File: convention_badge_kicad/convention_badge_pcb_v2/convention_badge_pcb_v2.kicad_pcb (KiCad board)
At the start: 2 copper layers, 5 parts, among them J2 ER-CON24HT-1, J3 3.7V Battery, SW4 SW_SPST, U1 ESP32-C3-WROOM-02

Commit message: schematic minus e paper integration complete
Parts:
- added C1: 1uf, PCM_JLCPCB:C_0603, F.Cu at (122.7, 65.8)
- added C2: 0.1uf, PCM_JLCPCB:C_0603, F.Cu at (122.7, 68.1)
- added C3: 10uf, PCM_JLCPCB:C_0603, F.Cu at (122.7, 70.3)
- added C4: 10uf, PCM_JLCPCB:C_0603, F.Cu at (122.7, 72.6)
- added C5: 0.1uF, PCM_JLCPCB:C_0603, F.Cu at (122.7, 74.8)
- added C6: 2.2uF, PCM_JLCPCB:C_0603, F.Cu at (122.7, 77.1)
- added C7: 100uF, PCM_JLCPCB:C_0603, F.Cu at (122.7, 79.3)
- added C8: 2.2uF, PCM_JLCPCB:C_0603, F.Cu at (122.7, 81.6)
- added C9: 0.1uF, PCM_JLCPCB:C_0603, F.Cu at (122.7, 83.8)
- added D2: LED, PCM_JLCPCB:D_0603, F.Cu at (179.4, 76.7)
- added D3: SS14, PCM_JLCPCB:D_DO-214AC(SMA), F.Cu at (100.0, 109.0)
- added DISP1: EPaper Breakout, 2_Displays:2.9_e_paper_ER-EPD029-2-5073, F.Cu at (83.6, 118.8)
- added J1: USBC, Connector_USB:USB_C_Receptacle_GCT_USB4105-xx-A_16P_TopMnt_Horizontal, F.Cu at (87.0, 101.0)
- added Q1: LP0404N3T5G, Package_TO_SOT_SMD:SOT-883, F.Cu at (178.0, 81.3)
- added R1: 5.1k, PCM_JLCPCB:R_0603, F.Cu at (131.6, 65.8)
- added R10: 100k, PCM_JLCPCB:R_0603, F.Cu at (135.2, 72.6)
- added R2: 5.1k, PCM_JLCPCB:R_0603, F.Cu at (131.6, 68.1)
- added R3: 10k, PCM_JLCPCB:R_0603, F.Cu at (131.6, 70.3)
- added R4: 10k, PCM_JLCPCB:R_0603, F.Cu at (131.6, 72.6)
- added R5: 1k, PCM_JLCPCB:R_0603, F.Cu at (131.6, 74.8)
- added R6: 1k, PCM_JLCPCB:R_0603, F.Cu at (131.6, 77.1)
- added R7: 10k, PCM_JLCPCB:R_0603, F.Cu at (135.2, 65.8)
- added R8: 100, PCM_JLCPCB:R_0603, F.Cu at (135.2, 68.1)
- added R9: 1k, PCM_JLCPCB:R_0603, F.Cu at (135.2, 70.3)
- added SW1: SW4X2, PCM_JLCPCB:SW-SMD_4P-L5.1-W5.1-P3.70-LS6.5-TL-2, F.Cu at (150.7, 97.2)
- added SW2: SW4X2, PCM_JLCPCB:SW-SMD_4P-L5.1-W5.1-P3.70-LS6.5-TL-2, F.Cu at (151.0, 104.0)
- added SW3: SW_Push, Button_Switch_THT:SW_PUSH_6mm, F.Cu at (176.5, 107.5)
- added SW5: SW_Push, Button_Switch_THT:SW_PUSH_6mm, F.Cu at (155.5, 148.5)
- added SW6: SW_SPST, Button_Switch_THT:SW_Slide-03_Wuerth-WS-SLTV_10x2.5x6.4_P2.54mm, F.Cu at (170.9, 82.1)
- added SW7: SW_Push, Button_Switch_THT:SW_PUSH_6mm, F.Cu at (124.5, 147.8)
- added SW8: SW_Push, Button_Switch_THT:SW_PUSH_6mm, F.Cu at (86.8, 146.8)
- added U2: FS8205A, Package_TO_SOT_SMD:SOT-23-6, F.Cu at (127.2, 67.1)
- added U3: TP4056, PCM_JLCPCB:ESOP-8_L4.9-W3.9-P1.27-LS6.0-BL-EP, F.Cu at (161.3, 68.7)
- added U4: DW01A, Package_TO_SOT_SMD:SOT-23-6, F.Cu at (127.2, 71.8)
- added U5: TLV75733PDBV, Package_TO_SOT_SMD:SOT-23-5, F.Cu at (127.2, 76.4)
- D1: value EPaper Display -> LED; footprint 2_Displays:2.9_e_paper_ER-EPD029-2-5073 -> PCM_JLCPCB:D_0603
- J2: value ER-CON24HT-1 -> EPaper; moved to B.Cu
- SW4: value SW_SPST -> SW_Push; footprint Button_Switch_THT:SW_Slide-03_Wuerth-WS-SLTV_10x2.5x6.4_P2.54mm -> Button_Switch_THT:SW_PUSH_6mm
- U1: moved to B.Cu
- moved D1 124.6 mm to (179.4, 74.1)
- moved SW4 85.7 mm to (175.5, 95.5)
- moved J2 82.4 mm to (168.6, 124.3), turned to 90 degrees
- moved J3 64.5 mm to (150.0, 114.5)
- moved U1 58.0 mm to (127.0, 100.6), turned to 180 degrees
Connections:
- D1 pad 1: +3.3V -> Net-(D1-K)
- D1 pad 2: GND -> /VUSB
- J3 pad 1: +3.7V -> Net-(J3-Pin_1)
- J3 pad 2: GND -> Net-(J3-Pin_2)
- SW4 pad 1: unconnected-(SW4-A-Pad1) -> /GPIO1
- SW4 pad 2: +3.7V -> GND
- U1 pad 11: unconnected-(U1-GPIO20/U0RXD-Pad11) -> /GPIO20
- U1 pad 12: unconnected-(U1-GPIO21/U0TXD-Pad12) -> /GPIO21
- U1 pad 15: unconnected-(U1-GPIO3/ADC1_CH3-Pad15) -> /GPIO3
- U1 pad 17: unconnected-(U1-GPIO1/ADC1_CH1/XTAL_32K_N-Pad17) -> /GPIO1
- U1 pad 18: unconnected-(U1-GPIO0/ADC1_CH0/XTAL_32K_P-Pad18) -> /GPIO0
- U1 pad 3: unconnected-(U1-GPIO4/ADC1_CH4-Pad3) -> /GPIO4
- U1 pad 4: unconnected-(U1-GPIO5/ADC2_CH0-Pad4) -> /GPIO5
- U1 pad 5: unconnected-(U1-GPIO6-Pad5) -> /GPIO6
- U1 pad 6: unconnected-(U1-GPIO7-Pad6) -> /GPIO7

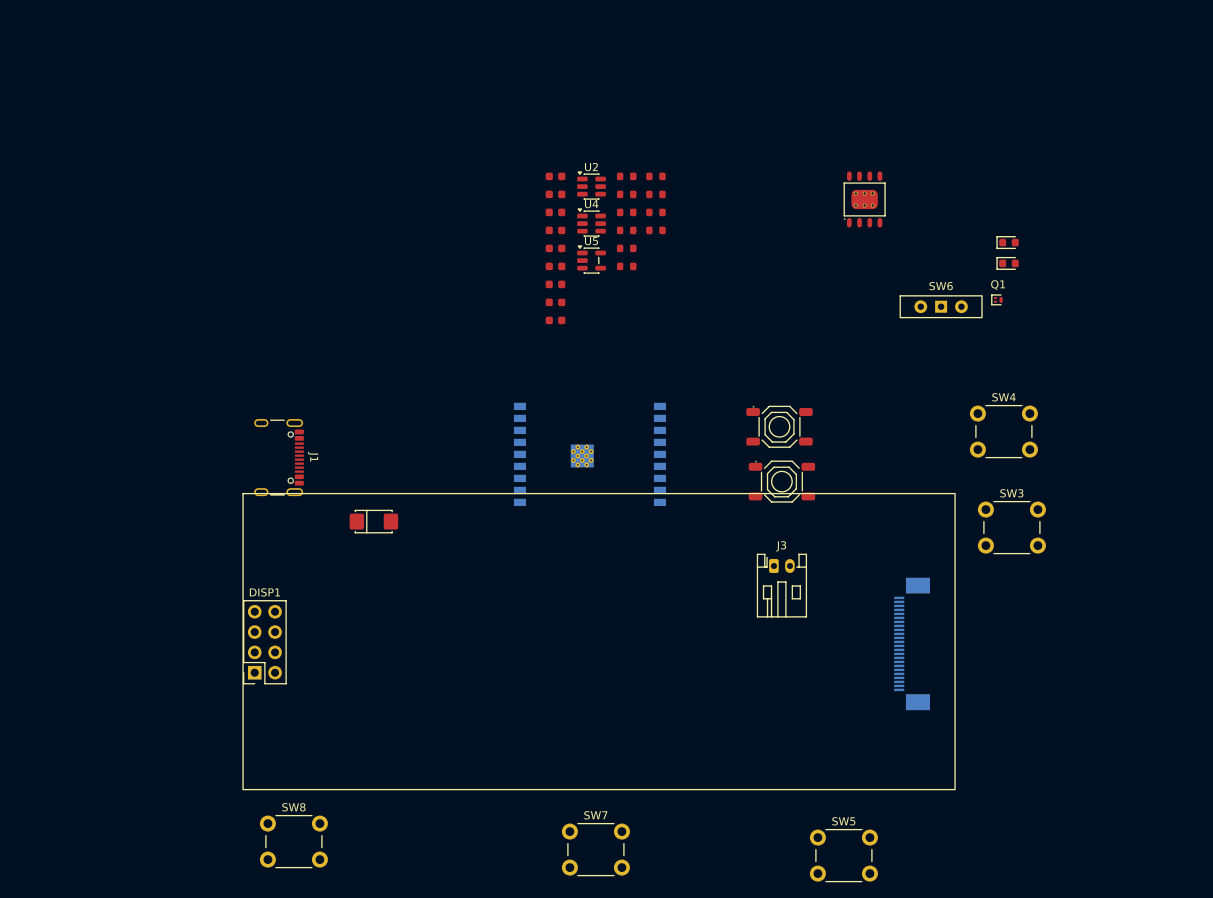
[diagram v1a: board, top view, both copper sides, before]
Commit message: layout is almost complete, kind of a rats nest
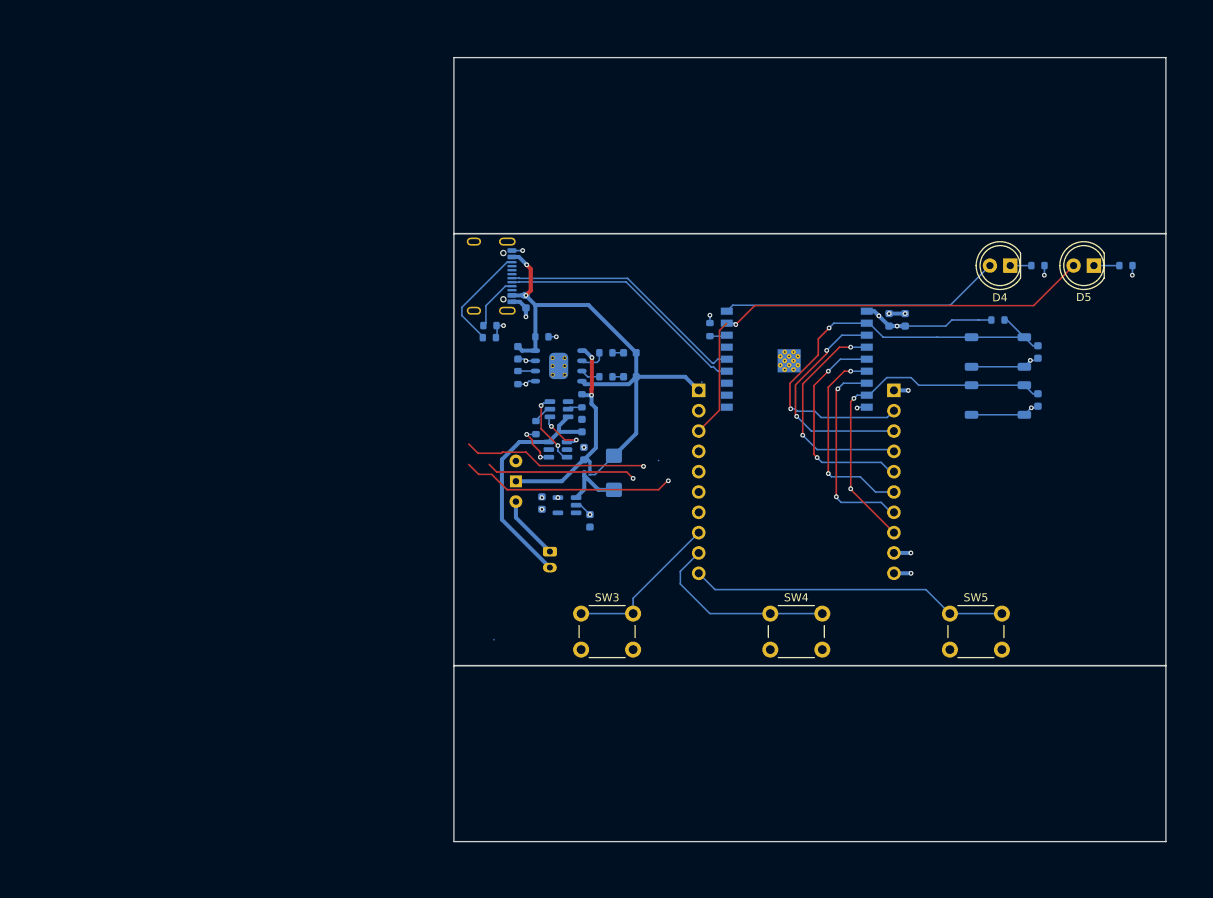
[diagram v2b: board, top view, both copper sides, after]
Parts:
- removed DISP1: EPaper Breakout, 2_Displays:2.9_e_paper_ER-EPD029-2-5073
- removed J2: EPaper, eastrising:ER-CON24HT-1
- removed SW7, SW8: SW_Push, Button_Switch_THT:SW_PUSH_6mm
- added C10: 10uF, PCM_JLCPCB:C_0603, B.Cu at (164.4, 83.8)
- added D4: LED, LED_THT:LED_D5.0mm, F.Cu at (179.5, 77.0)
- added D5: LED, LED_THT:LED_D5.0mm, F.Cu at (190.0, 77.0)
- added J4: Conn_01x10_Pin, Connector_PinHeader_2.54mm:PinHeader_1x10_P2.54mm_Vertical, B.Cu at (165.0, 92.6)
- added J5: Conn_01x10_Pin, Connector_PinHeader_2.54mm:PinHeader_1x10_P2.54mm_Vertical, B.Cu at (140.6, 92.6)
- added R11: 1k, PCM_JLCPCB:R_0603, B.Cu at (183.0, 77.0)
- added R12: 1k, PCM_JLCPCB:R_0603, B.Cu at (194.0, 77.0)
- C1, C2, C3, C4, C5, C6, C7, C8, C9, D1, D2, D3, J1, J3, Q1, R1, R2, R3, R4, R5, R6, R8, R9, SW1, SW2, SW6, U2, U3, U4, U5: moved to B.Cu
- R10: value 100k -> 10k; moved to B.Cu
- R7: value 10k -> 2.2k; moved to B.Cu
- moved C2 65.5 mm to (183.0, 93.8), turned to -90 degrees
- moved C1 64.2 mm to (183.0, 87.8), turned to -90 degrees
- moved SW6 57.5 mm to (117.8, 104.0), turned to 90 degrees
- moved Q1 55.8 mm to (126.7, 102.9), turned to 180 degrees
- moved SW3 52.2 mm to (125.9, 120.5)
- moved D1 50.3 mm to (132.0, 90.9)
- moved D2 48.7 mm to (132.0, 87.9)
- moved R3 48.3 mm to (178.0, 83.8)
- moved C9 43.7 mm to (166.4, 83.8), turned to 90 degrees
- moved U3 43.5 mm to (123.1, 89.5), turned to 90 degrees
- moved SW4 36.0 mm to (149.6, 120.5)
- moved J1 34.9 mm to (113.6, 78.3), turned to 90 degrees
- moved U2 33.1 mm to (123.0, 100.0)
- moved SW5 32.5 mm to (172.0, 120.5)
- moved C6 32.1 mm to (127.0, 108.9), turned to 90 degrees
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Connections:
- net +3.7V renamed /VBAT
- SW3 pad 1: /GPIO0 -> /GPIO21
- SW4 pad 1: /GPIO1 -> /GPIO20
- SW5 pad 1: /GPIO20 -> /GPIO10
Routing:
- net /GPIO9: track 0.00 -> 96.1 mm, vias 0 -> 3
- net /GPIO8: track 0.00 -> 73.8 mm, vias 0 -> 3
- net /GPIO7: track 0.00 -> 73.4 mm, vias 0 -> 3
- net /GPIO4: track 0.00 -> 70.7 mm, vias 0 -> 2
- net /GPIO5: track 0.00 -> 70.5 mm, vias 0 -> 2
- net /GPIO6: track 0.00 -> 69.9 mm, vias 0 -> 2
- net /VUSB: track 0.00 -> 67.5 mm, vias 0 -> 2
- net /GPIO1: track 0.00 -> 61.4 mm, vias 0 -> 1
- net /EN: track 0.00 -> 57.1 mm, vias 0 -> 2
- net GND: track 0.00 -> 40.2 mm, vias 0 -> 17
- net /GPIO10: track 0.00 -> 40.0 mm
- net /GPIO0: track 0.00 -> 35.3 mm
- net /USB_D-: track 0.00 -> 31.5 mm
- net /USB_D+: track 0.00 -> 31.5 mm
- net Net-(J3-Pin_2): track 0.00 -> 29.8 mm
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- added copper zone on In1.Cu, net +3.3V
- added copper zone on In2.Cu, net GND
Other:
- board outline added: 89 x 98 mm
- copper layers 2 -> 4

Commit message: cleaned up layout and seperated breakout headers.
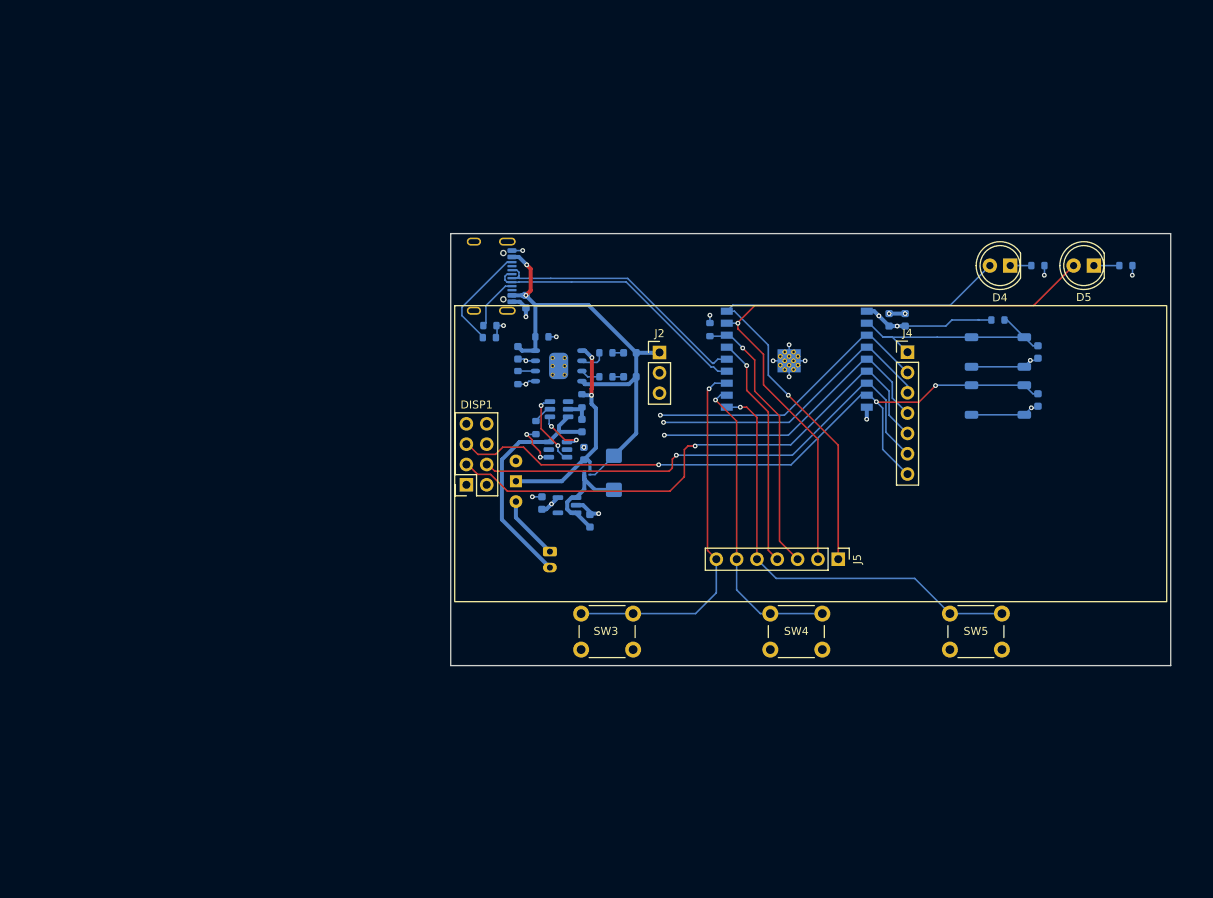
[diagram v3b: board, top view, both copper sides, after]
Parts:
- added DISP1: EPaper Breakout, 2_Displays:2.9_e_paper_ER-EPD029-2-5073, F.Cu at (110.1, 95.3)
- added J2: Conn_01x03_Pin, Connector_PinHeader_2.54mm:PinHeader_1x03_P2.54mm_Vertical, F.Cu at (135.7, 87.9)
- J4, J5: value Conn_01x10_Pin -> Conn_01x07_Pin; footprint Connector_PinHeader_2.54mm:PinHeader_1x10_P2.54mm_Vertical -> Connector_PinHeader_2.54mm:PinHeader_1x07_P2.54mm_Vertical; moved to F.Cu
- moved J5 27.4 mm to (158.0, 113.7), turned to -90 degrees
- moved J4 5.07 mm to (166.7, 87.8), turned to 0 degrees
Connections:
- J4 pad 1: +3.3V -> /EN
- J4 pad 2: /EN -> /GPIO4
- J4 pad 3: /GPIO4 -> /GPIO5
- J4 pad 4: /GPIO5 -> /GPIO6
- J4 pad 5: /GPIO6 -> /GPIO7
- J4 pad 6: /GPIO7 -> /GPIO8
- J4 pad 7: /GPIO8 -> /GPIO9
- J5 pad 1: /VUSB -> /GPIO0
- J5 pad 2: /GPIO0 -> /GPIO1
- J5 pad 3: /GPIO1 -> /GPIO2
- J5 pad 4: /GPIO2 -> /GPIO3
- J5 pad 5: /GPIO3 -> /GPIO10
- J5 pad 6: /USB_D+ -> /GPIO20
- J5 pad 7: /USB_D- -> /GPIO21
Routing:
- net /GPIO0: track 35.3 -> 72.9 mm, vias 0 -> 1
- net /GPIO2: track 2.16 -> 34.1 mm, vias 0 -> 1
- net /GPIO3: track 0.00 -> 29.2 mm, vias 0 -> 1
- net /EN: track 57.1 -> 30.0 mm, vias 2 -> 0
- net /GPIO21: track 20.0 -> 46.5 mm, vias 0 -> 1
- net /GPIO1: track 61.4 -> 80.0 mm
- net /GPIO10: track 40.0 -> 55.5 mm, vias 0 -> 1
- net /GPIO20: track 25.1 -> 38.7 mm, vias 0 -> 1
- net /GPIO5: track 70.5 -> 60.8 mm, vias 2 -> 1
- net /GPIO8: track 73.8 -> 64.1 mm, vias 3 -> 1
- net /GPIO4: track 70.7 -> 61.7 mm, vias 2 -> 1
- net /GPIO6: track 69.9 -> 61.2 mm, vias 2 -> 1
- net GND: track 40.2 -> 48.5 mm, vias 17 -> 20
- net /GPIO9: track 96.1 -> 89.4 mm
- net Net-(D3-K): track 8.31 -> 14.7 mm
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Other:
- board size 89 x 98 mm -> 90 x 54 mm

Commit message: made board outline
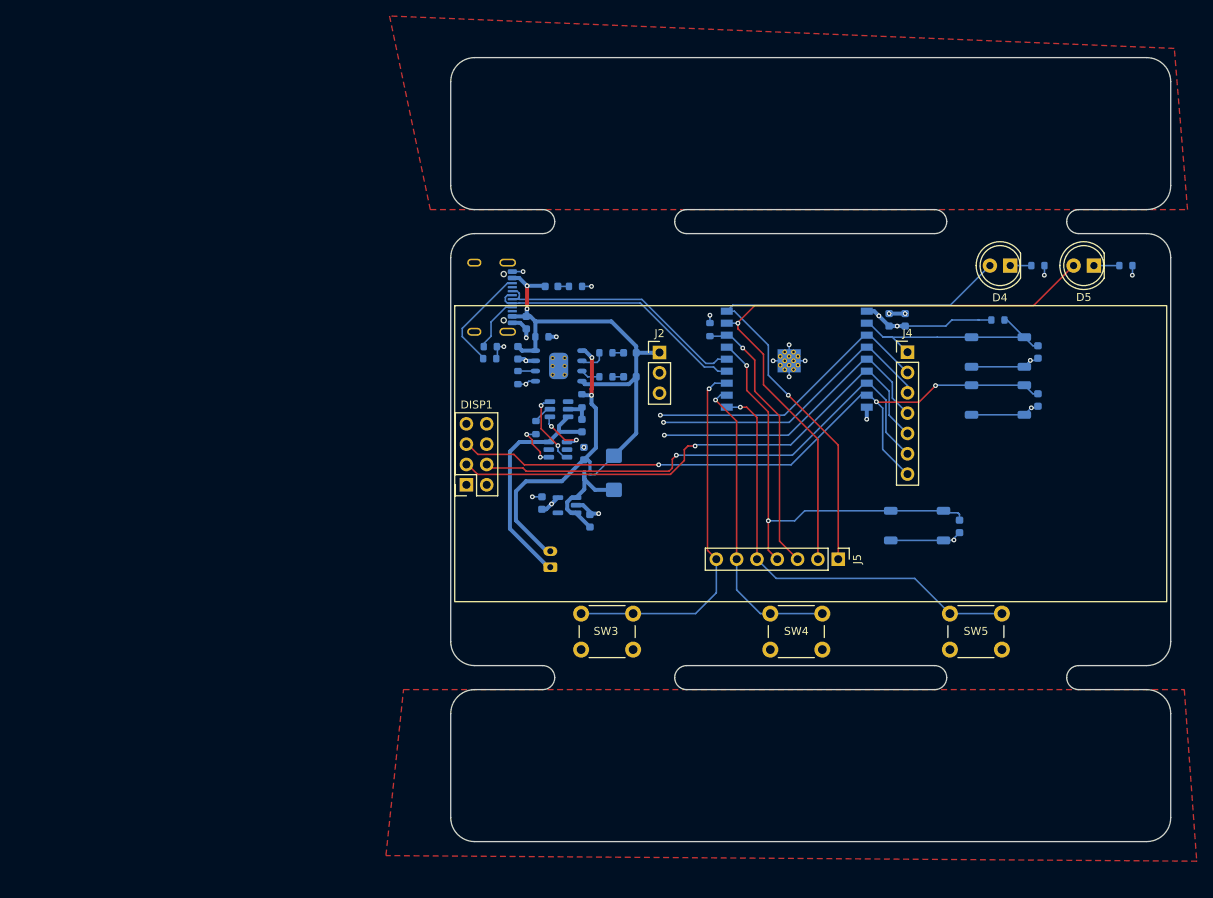
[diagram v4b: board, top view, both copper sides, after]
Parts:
- added C11: 0.1uf, PCM_JLCPCB:C_0603, B.Cu at (173.2, 109.6)
- added D7: LED, PCM_JLCPCB:D_0603, B.Cu at (122.2, 79.6)
- added R13: 1k, PCM_JLCPCB:R_0603, B.Cu at (125.2, 79.6)
- SW6: value SW_SPST -> SW4X2; footprint Button_Switch_THT:SW_Slide-03_Wuerth-WS-SLTV_10x2.5x6.4_P2.54mm -> PCM_JLCPCB:SW-SMD_4P-L5.1-W5.1-P3.70-LS6.5-TL-2
- moved SW6 50.5 mm to (167.9, 109.5), turned to 0 degrees
- moved J1 2.63 mm to (113.6, 81.0)
- moved C7 2.63 mm to (119.0, 84.1)
- moved R1 2.63 mm to (114.5, 87.1)
- moved R2 2.63 mm to (114.5, 88.6)
- moved J3 1.95 mm to (122.0, 114.7), turned to 90 degrees
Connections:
- C5 pad 2: Net-(J3-Pin_2) -> Net-(J3-Pin_1)
- J3 pad 2: Net-(J3-Pin_2) -> /VBAT
- SW6 pad 1: /VBAT -> GND
- SW6 pad 2: Net-(J3-Pin_1) -> GND
- SW6 pad 3: (no net) -> /GPIO3
- U2 pad 3: Net-(J3-Pin_2) -> Net-(J3-Pin_1)
- U4 pad 6: Net-(J3-Pin_2) -> Net-(J3-Pin_1)
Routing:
- net Net-(J3-Pin_2): track 29.8 -> 0.00 mm
- net /GPIO3: track 29.2 -> 54.5 mm, vias 1 -> 2
- net Net-(J3-Pin_1): track 8.01 -> 29.1 mm
- net GND: track 48.5 -> 58.8 mm, vias 20 -> 22
- net /VBAT: track 28.1 -> 38.1 mm
- net /GPIO7: track 69.6 -> 66.7 mm
- net Net-(D7-K): track 0.00 -> 1.39 mm
- net /USB_D+: track 33.9 -> 32.8 mm
- net /USB_D-: track 33.9 -> 32.8 mm
- net /VUSB: track 61.9 -> 60.8 mm
- net /GPIO9: track 89.4 -> 88.7 mm
- added copper zone on F.Cu, net (none)
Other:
- board size 90 x 54 mm -> 90 x 98 mm
